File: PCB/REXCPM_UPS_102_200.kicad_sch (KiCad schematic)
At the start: 7 parts, among them J1 Model_100_System_BUS, J2 Conn_01x03_Pin, U1 742G02

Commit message: add version for tandy 102 & 200
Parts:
- removed J1: Model_100_System_BUS, 000_LOCAL:DIP-40_pins, symbol 000_LOCAL:Model_100_System_BUS
- added J3: Conn_02x20_Odd_Even, 000_LOCAL:IDC-Header_2x20_P2.54mm_Vertical, symbol 000_LOCAL:Conn_02x20_Odd_Even
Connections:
- net A15: now also U1.5, U1.6, J3.19 (Pin_19); no longer U1.1, U1.2
- net BATT+: now also D1.2; no longer D1.1
- net GND: now also J3.21 (Pin_21), J3.22 (Pin_22), J3.3 (Pin_3), J3.35 (Pin_35), J3.36 (Pin_36), J3.4 (Pin_4)
- net IO/~{M}: now also U1.1, J3.26 (Pin_26); no longer U1.5
- net RAM: now also U1.7; no longer U1.3
- net RAM_RST: now also J3.38 (Pin_38)
- net VBUS: now also D1.1, J3.1 (Pin_1), J3.2 (Pin_2); no longer D1.2
- net ~{WR}: now also J3.23 (Pin_23)
- new net: U1.2, U1.3
- no-connect marks 25 -> 28
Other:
- note added: "A10"
- note added: "A11"
- note added: "A12"
- note added: "A13"
- note added: "A14"
- note added: "A8"
- note added: "A9"
- note added: "AD0"
- note added: "AD1"
- note added: "AD2"
- note added: "AD3"
- note added: "AD4"
- note added: "AD5"
- note added: "AD6"
- note added: "AD7"
- note added: "CLK"
- note added: "GND"
- note added: "INTA"
- note added: "INTR"
- note added: "NC"
- note added: "S0"
- note added: "S1"
- note added: "TANDY 102/200 SYSTEM BUS"
- note added: "VDD"
- note added: "Y0"
- note added: "~{ALE}"
- note added: "~{A}"
- note added: "~{RD}"
- note added: "~{RESET}"
- title: REXCPM UPS -> REXCPM UPS 102/200
- moved on the sheet: J2, U1A, U1B

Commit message: fix 102_200 name
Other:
- title: REXCPM UPS 102/200 -> REXCPM UPS 102_200
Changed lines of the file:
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@@
   (paper "USLetter")
   (title_block
-    (title "REXCPM UPS 102/200")
+    (title "REXCPM UPS 102_200")
     (date "2023-09-02")
     (rev "001")

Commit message: readme
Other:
- note added: "system bus connection shown using the standard pin numbers for the connector, not the odd<>even switched pin numbers in the Tandy 102 & 200 manuals."
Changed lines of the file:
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@@
+    (effects (font (size 1.27 1.27)) (justify left bottom))
+  )
+  (text "system bus connection shown using the standard pin numbers for the connector,\nnot the odd<>even switched pin numbers in the Tandy 102 & 200 manuals."
+    (at 17.78 198.12 0)
     (effects (font (size 1.27 1.27)) (justify left bottom))
   )

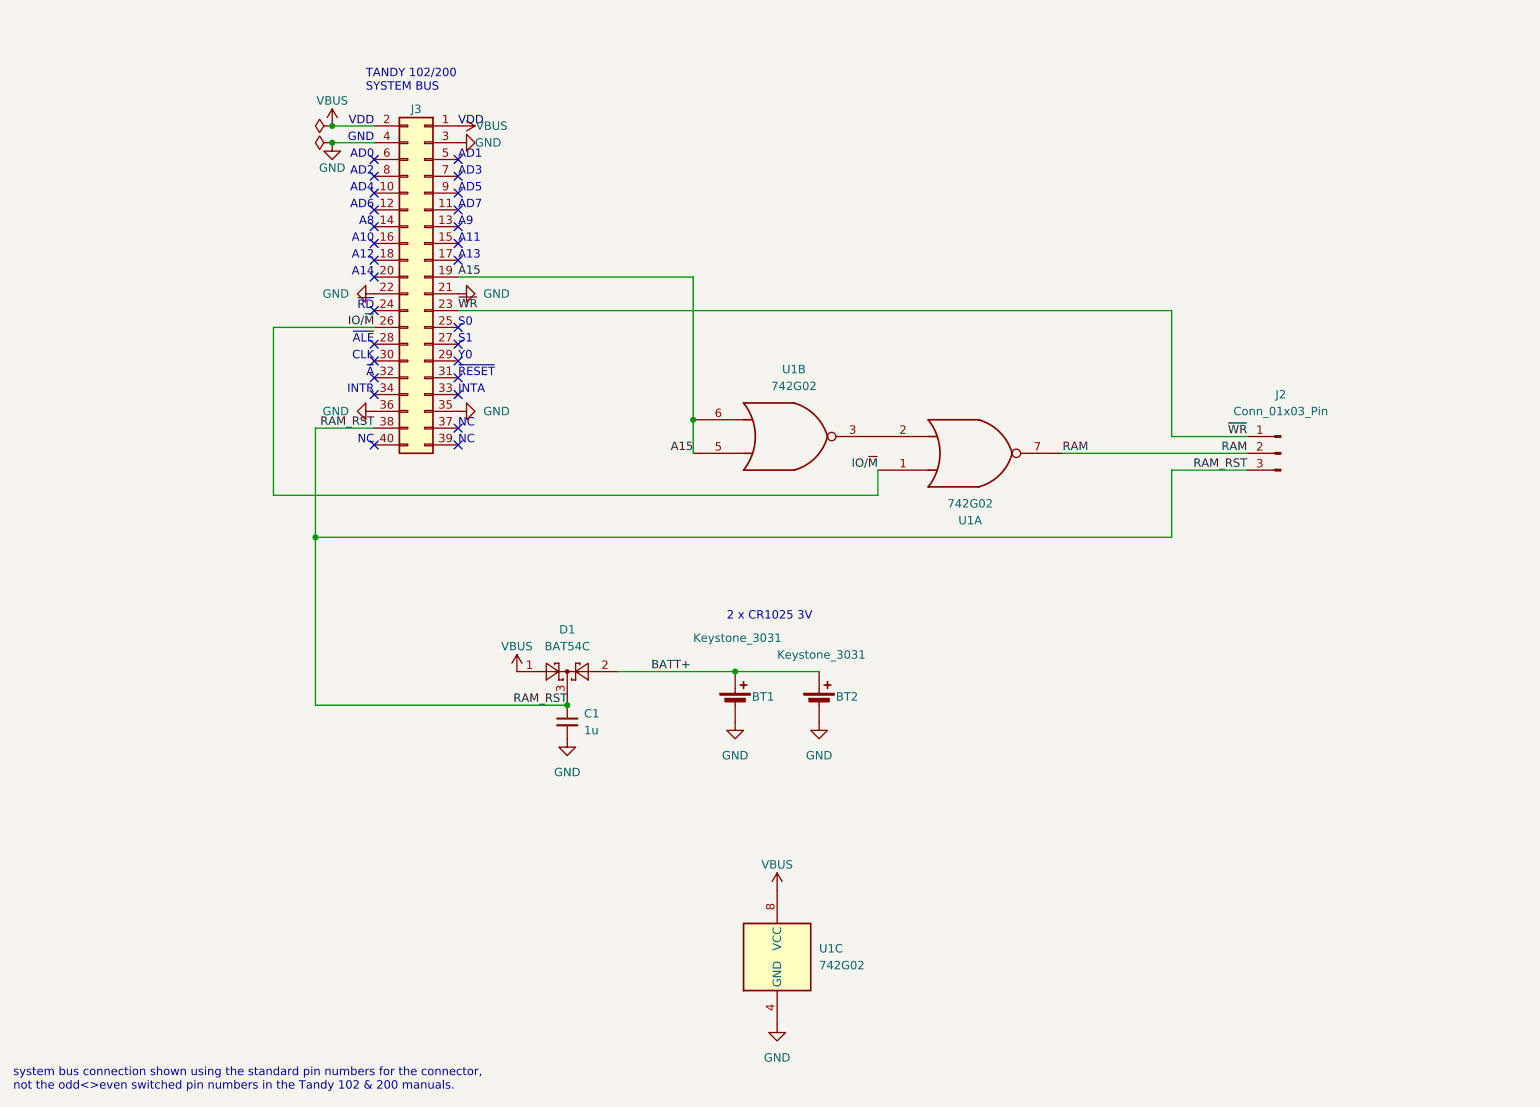
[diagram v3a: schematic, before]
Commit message: 4-cells, add gnd wire, jst-sh connector
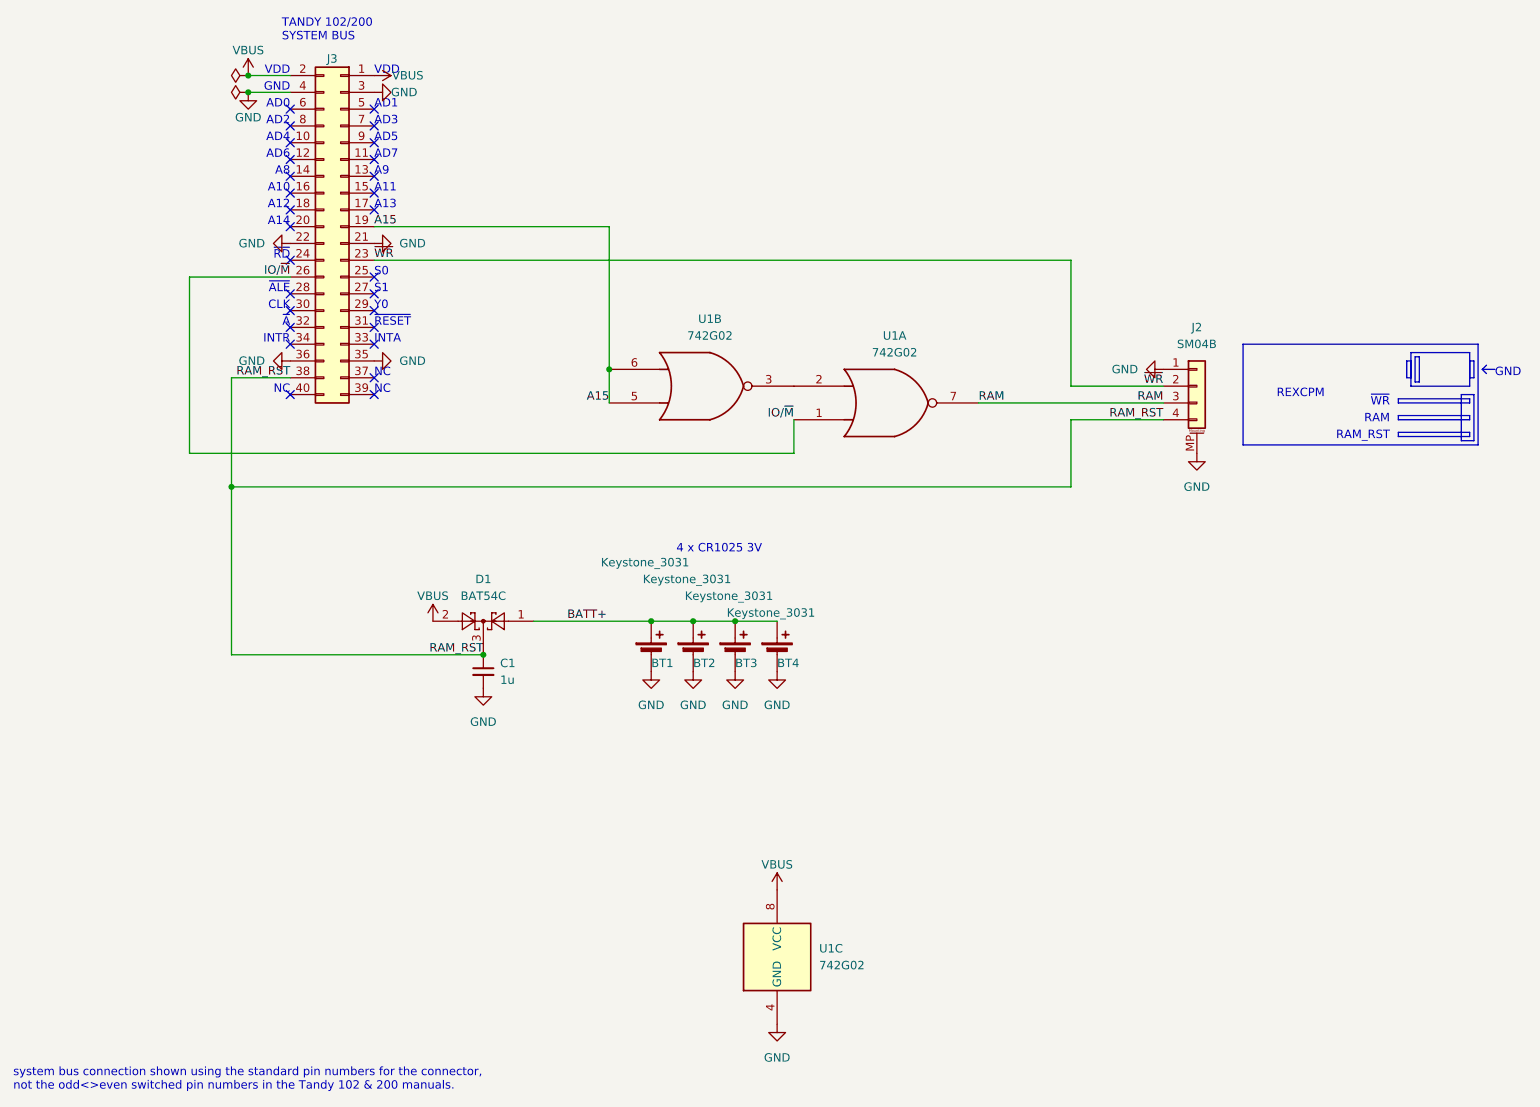
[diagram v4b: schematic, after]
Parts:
- added BT3, BT4: Keystone_3031, 000_LOCAL:Keystone_3031, symbol 000_LOCAL:Battery_Cell
- J2: value Conn_01x03_Pin -> SM04B; footprint 000_LOCAL:PinHeader_1x03_P2.54mm_Horizontal -> 000_LOCAL:JST_SH_SM04B-SRSS-TB_1x04-1MP_P1.00mm_Horizontal; symbol 000_LOCAL:Conn_01x03_Pin -> 000_LOCAL:Conn_01x04_MountingPin
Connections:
- net BATT+: now also D1.1, BT3.1 (+), BT4.1 (+); no longer D1.2
- net GND: now also J2.1 (Pin_1), J2.MP (MountPin), BT3.2 (-), BT4.2 (-)
- net RAM: now also J2.3 (Pin_3); no longer J2.2 (Pin_2)
- net RAM_RST: now also J2.4 (Pin_4); no longer J2.3 (Pin_3)
- net VBUS: now also D1.2; no longer D1.1
- net ~{WR}: now also J2.2 (Pin_2); no longer J2.1 (Pin_1)
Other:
- note added: "4 x CR1025 3V"
- note added: "RAM"
- note added: "RAM_RST"
- note added: "REXCPM"
- note added: "~{WR}"
- note removed: "2 x CR1025 3V"
- moved on the sheet: BT1, BT2, C1, D1, J3, U1A, U1B
